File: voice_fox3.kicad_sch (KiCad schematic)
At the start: 9 parts, among them J2 SJ1-2503A, J3 SJ1-3533NG, Q1 2N3904, U1 DFR0299

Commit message: added audio in to mcu ADC
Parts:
- added R3, R4: 10K, Resistor_THT:R_Axial_DIN0207_L6.3mm_D2.5mm_P10.16mm_Horizontal, symbol Device:R
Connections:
- net GND: now also R3.2
- net at C1.1: now also A2.J1_1 (A0), R3.1, R4.2
- net at C1.2: now also J2.3
- net +3.3V: now reaches A2.J2_15 (3V3), A2.J2_6 (3V3), U1.1 (VCC)
- net +3.3V: now also A2.J1_11 (3V3), R4.1
- no-connect marks 32 -> 29
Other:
- note added: "Radio Audio In"
- moved on the sheet: A2A, C1

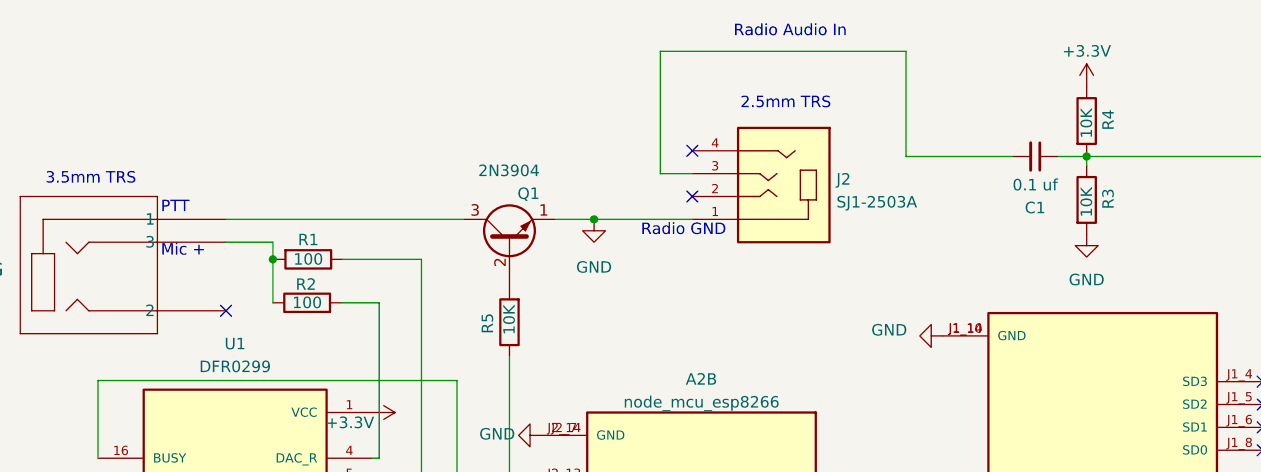
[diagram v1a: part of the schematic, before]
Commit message: added audio in to mcu ADC, added 3v3 net
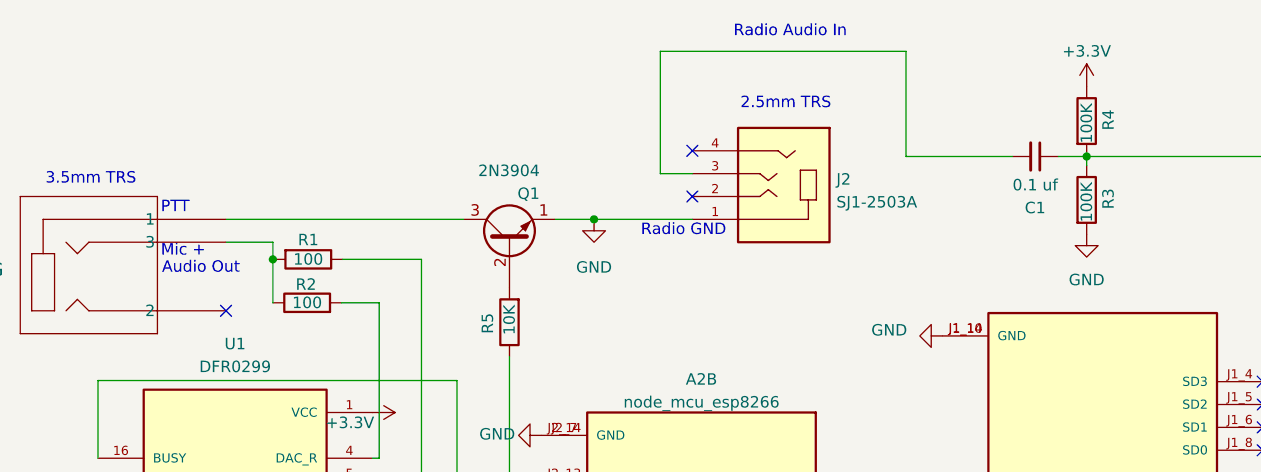
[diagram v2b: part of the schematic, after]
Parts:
- R3, R4: value 10K -> 100K
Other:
- note added: "Audio Out"
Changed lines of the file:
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@@
+    (effects (font (size 1.27 1.27)) (justify left bottom))
+  )
+  (text "Audio Out" (at 81.915 89.789 0)
     (effects (font (size 1.27 1.27)) (justify left bottom))
   )
@@
       (effects (font (size 1.27 1.27)))
     )
-    (property "Value" "10K" (at 184.658 72.898 90)
+    (property "Value" "100K" (at 184.658 72.898 90)
       (effects (font (size 1.27 1.27)))
     )
@@
       (effects (font (size 1.27 1.27)))
     )
-    (property "Value" "10K" (at 184.658 81.661 90)
-      (effects (font (size 1.27 1.27)))
-    )
+    (property "Value" "100K" (at 184.658 81.661 90)
+      (effects (font (size 1.27 1.27)))
+    )

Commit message: many changes
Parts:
- added J1: 2 pin 2mm JST, JST_B2B-PH-K-S(LF)(SN), symbol JST 2pin 2mm jack:B2B-PH-K-S(LF)(SN)
- Q1: footprint Package_TO_SOT_THT:TO-92_Inline -> Package_TO_SOT_THT:TO-92_HandSolder
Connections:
- net GND: now also J1.2
- net at A2.J1_15 (VIN): now also J1.1
- no-connect marks 29 -> 28
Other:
- moved on the sheet: A2A
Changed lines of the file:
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@@
   (junction (at 94.234 88.011) (diameter 0) (color 0 0 0 0)
   )
-  (no_connect (at 204.216 106.68))
+  (no_connect (at 204.851 117.475))
   (no_connect (at 74.803 132.969))
-  (no_connect (at 204.216 124.46))
-  (no_connect (at 204.216 104.14))
-  (no_connect (at 168.656 116.84))
+  (no_connect (at 204.851 135.255))
+  (no_connect (at 204.851 114.935))
+  (no_connect (at 169.291 127.635))
   (no_connect (at 124.079 117.729))
-  (no_connect (at 168.656 119.38))
+  (no_connect (at 169.291 130.175))
   (no_connect (at 74.803 115.189))
   (no_connect (at 74.803 130.429))
@@
   (no_connect (at 159.639 120.269))
   (no_connect (at 105.283 125.349))
-  (no_connect (at 204.216 109.22))
+  (no_connect (at 204.851 120.015))
   (no_connect (at 140.843 75.946))
-  (no_connect (at 204.216 116.84))
+  (no_connect (at 204.851 127.635))
   (no_connect (at 74.803 125.349))
-  (no_connect (at 204.216 114.3))
+  (no_connect (at 204.851 125.095))
   (no_connect (at 159.639 115.189))
   (no_connect (at 74.803 122.809))
-  (no_connect (at 204.216 101.6))
-  (no_connect (at 204.216 127))
+  (no_connect (at 204.851 112.395))
+  (no_connect (at 204.851 137.795))
   (no_connect (at 159.639 122.809))
-  (no_connect (at 168.656 134.62))
   (wire (pts (xy 89.027 86.106) (xy 94.234 86.106))
     (stroke (width 0) (type default))
   )
-  (wire (pts (xy 210.82 119.38) (xy 210.82 76.581))
+  (wire (pts (xy 210.82 130.175) (xy 210.82 76.581))
     (stroke (width 0) (type default))
   )
@@
     (stroke (width 0) (type default))
   )
-  (wire (pts (xy 204.216 119.38) (xy 210.82 119.38))
+  (wire (pts (xy 204.851 130.175) (xy 210.82 130.175))
     (stroke (width 0) (type default))
   )
@@
   )
   (wire (pts (xy 94.234 88.011) (xy 94.361 88.011))
+    (stroke (width 0) (type default))
+  )
+  (wire (pts (xy 152.908 145.415) (xy 169.291 145.415))
     (stroke (width 0) (type default))
   )
@@
     )
   )
-  (symbol (lib_name "GND_2") (lib_id "power:GND") (at 168.656 96.52 270) (unit 1)
-    (in_bom yes) (on_board yes) (dnp no) (fields_autoplaced)
-    (property "Reference" "#PWR02" (at 162.306 96.52 0)
-      (effects (font (size 1.27 1.27)) hide)
-    )
-    (property "Value" "GND" (at 164.719 95.885 90)
+  (symbol (lib_id "power:GND") (at 152.908 142.875 180) (unit 1)
+    (in_bom yes) (on_board yes) (dnp no) (fields_autoplaced)
+    (property "Reference" "#PWR012" (at 152.908 136.525 0)
+      (effects (font (size 1.27 1.27)) hide)
+    )
+    (property "Value" "GND" (at 152.908 138.43 0)
+      (effects (font (size 1.27 1.27)))
+    )
+    (property "Footprint" "" (at 152.908 142.875 0)
+      (effects (font (size 1.27 1.27)) hide)
+    )
+    (property "Datasheet" "" (at 152.908 142.875 0)
+      (effects (font (size 1.27 1.27)) hide)
+    )
+    (pin "1")
+    (instances
+      (project "voice_fox3"
+        (path "/0bd27f7b-372b-41bd-a5d4-e6793a4f4a75"
+          (reference "#PWR012") (unit 1)
+        )
+      )
+    )
+  )
+  (symbol (lib_name "GND_2") (lib_id "power:GND") (at 169.291 107.315 270) (unit 1)
+    (in_bom yes) (on_board yes) (dnp no) (fields_autoplaced)
+    (property "Reference" "#PWR02" (at 162.941 107.315 0)
+      (effects (font (size 1.27 1.27)) hide)
+    )
+    (property "Value" "GND" (at 165.354 106.68 90)
       (effects (font (size 1.27 1.27)) (justify right))
     )
-    (property "Footprint" "" (at 168.656 96.52 0)
-      (effects (font (size 1.27 1.27)) hide)
-    )
-    (property "Datasheet" "" (at 168.656 96.52 0)
+    (property "Footprint" "" (at 169.291 107.315 0)
+      (effects (font (size 1.27 1.27)) hide)
+    )
+    (property "Datasheet" "" (at 169.291 107.315 0)
       (effects (font (size 1.27 1.27)) hide)
     )
@@
   (symbol (lib_id "Device:R") (at 184.658 72.644 0) (unit 1)
     (in_bom yes) (on_board yes) (dnp no)
-    (property "Reference" "R4" (at 187.071 72.517 90)
+    (property "Reference" "R4" (at 182.626 72.517 90)
       (effects (font (size 1.27 1.27)))
     )
@@
     )
   )
-  (symbol (lib_id "power:+3.3V") (at 168.656 132.08 90) (unit 1)
-    (in_bom yes) (on_board yes) (dnp no)
-    (property "Reference" "#PWR09" (at 172.466 132.08 0)
-      (effects (font (size 1.27 1.27)) hide)
-    )
-    (property "Value" "+3.3V" (at 165.735 132.207 90)
+  (symbol (lib_id "JST 2pin 2mm jack:B2B-PH-K-S(LF)(SN)") (at 145.288 145.415 180) (unit 1)
+    (in_bom yes) (on_board yes) (dnp no)
+    (property "Reference" "J1" (at 141.986 145.415 0)
       (effects (font (size 1.27 1.27)) (justify left))
     )
-    (property "Footprint" "" (at 168.656 132.08 0)
-      (effects (font (size 1.27 1.27)) hide)
-    )
-    (property "Datasheet" "" (at 168.656 132.08 0)
+    (property "Value" "2 pin 2mm JST" (at 152.908 149.225 0)
+      (effects (font (size 1.27 1.27)) (justify left))
+    )
+    (property "Footprint" "JST_B2B-PH-K-S(LF)(SN)" (at 145.288 145.415 0)
+      (effects (font (size 1.27 1.27)) (justify bottom) hide)
+    )
+    (property "Datasheet" "" (at 145.288 145.415 0)
+      (effects (font (size 1.27 1.27)) hide)
+    )
+    (property "MF" "JST Sales" (at 145.288 145.415 0)
+      (effects (font (size 1.27 1.27)) (justify bottom) hide)
+    )
+    (property "DIGI-KEY_PURCHASE_URL" "https://www.digikey.com.ua/product-detail/en/jst-sales-america-inc/B2B-PH-K-S_LF__SN_/455-1704-ND/926611?utm_source=snapeda&utm_medium=aggregator&utm_campaign=symbol" (at 145.288 145.415 0)
+      (effects (font (size 1.27 1.27)) (justify bottom) hide)
+    )
+    (property "DESCRIPTION" "PH Series 2 Position 2 mm Pitch Through Hole Top Entry Shrouded Header" (at 145.288 145.415 0)
+      (effects (font (size 1.27 1.27)) (justify bottom) hide)
+    )
+    (property "PACKAGE" "None" (at 145.288 145.415 0)
+      (effects (font (size 1.27 1.27)) (justify bottom) hide)
+    )
+    (property "STANDARD" "IPC-7251" (at 145.288 145.415 0)
+      (effects (font (size 1.27 1.27)) (justify bottom) hide)
+    )
+    (property "PARTREV" "N/A" (at 145.288 145.415 0)
+      (effects (font (size 1.27 1.27)) (justify bottom) hide)
+    )
+    (property "MP" "B2B-PH-K-S_LF__SN_" (at 145.288 145.415 0)
+      (effects (font (size 1.27 1.27)) (justify bottom) hide)
+    )
+    (property "DIGI-KEY_PART_NUMBER" "455-1704-ND" (at 145.288 145.415 0)
+      (effects (font (size 1.27 1.27)) (justify bottom) hide)
+    )
+    (pin "1")
+    (pin "2")
+    (instances
+      (project "voice_fox3"
+        (path "/0bd27f7b-372b-41bd-a5d4-e6793a4f4a75"
+          (reference "J1") (unit 1)
+        )
+      )
+    )
+  )
+  (symbol (lib_id "power:+3.3V") (at 169.291 142.875 90) (unit 1)
+    (in_bom yes) (on_board yes) (dnp no)
+    (property "Reference" "#PWR09" (at 173.101 142.875 0)
+      (effects (font (size 1.27 1.27)) hide)
+    )
+    (property "Value" "+3.3V" (at 166.37 143.002 90)
+      (effects (font (size 1.27 1.27)) (justify left))
+    )
+    (property "Footprint" "" (at 169.291 142.875 0)
+      (effects (font (size 1.27 1.27)) hide)
+    )
+    (property "Datasheet" "" (at 169.291 142.875 0)
       (effects (font (size 1.27 1.27)) hide)
     )
@@
     )
   )
-  (symbol (lib_id "bills_library:node_mcu_esp8266") (at 186.436 116.84 180) (unit 1)
-    (in_bom yes) (on_board yes) (dnp no) (fields_autoplaced)
-    (property "Reference" "A2" (at 186.436 140.716 0)
-      (effects (font (size 1.27 1.27)))
-    )
-    (property "Value" "node_mcu_esp8266" (at 186.436 138.176 0)
-      (effects (font (size 1.27 1.27)))
-    )
-    (property "Footprint" "bills_library:node_mcu_esp8266" (at 186.436 116.84 0)
-      (effects (font (size 1.27 1.27)) (justify bottom) hide)
-    )
-    (property "Datasheet" "" (at 186.436 116.84 0)
-      (effects (font (size 1.27 1.27)) hide)
-    )
-    (property "PARTREV" "N/A" (at 186.436 116.84 0)
-      (effects (font (size 1.27 1.27)) (justify bottom) hide)
-    )
-    (property "STANDARD" "Manufacturer Recommendations" (at 186.436 116.84 0)
-      (effects (font (size 1.27 1.27)) (justify bottom) hide)
-    )
-    (property "MAXIMUM_PACKAGE_HEIGHT" "N/A" (at 186.436 116.84 0)
-      (effects (font (size 1.27 1.27)) (justify bottom) hide)
-    )
-    (property "MANUFACTURER" "Seeed" (at 186.436 116.84 0)
-      (effects (font (size 1.27 1.27)) (justify bottom) hide)
-    )
-    (property "Sim.Enable" "0" (at 186.436 116.84 0)
+  (symbol (lib_id "bills_library:node_mcu_esp8266") (at 187.071 127.635 180) (unit 1)
+    (in_bom yes) (on_board yes) (dnp no) (fields_autoplaced)
+    (property "Reference" "A2" (at 187.071 151.511 0)
+      (effects (font (size 1.27 1.27)))
+    )
+    (property "Value" "node_mcu_esp8266" (at 187.071 148.971 0)
+      (effects (font (size 1.27 1.27)))
+    )
+    (property "Footprint" "bills_library:node_mcu_esp8266" (at 187.071 127.635 0)
+      (effects (font (size 1.27 1.27)) (justify bottom) hide)
+    )
+    (property "Datasheet" "" (at 187.071 127.635 0)
+      (effects (font (size 1.27 1.27)) hide)
+    )
+    (property "PARTREV" "N/A" (at 187.071 127.635 0)
+      (effects (font (size 1.27 1.27)) (justify bottom) hide)
+    )
+    (property "STANDARD" "Manufacturer Recommendations" (at 187.071 127.635 0)
+      (effects (font (size 1.27 1.27)) (justify bottom) hide)
+    )
+    (property "MAXIMUM_PACKAGE_HEIGHT" "N/A" (at 187.071 127.635 0)
+      (effects (font (size 1.27 1.27)) (justify bottom) hide)
+    )
+    (property "MANUFACTURER" "Seeed" (at 187.071 127.635 0)
+      (effects (font (size 1.27 1.27)) (justify bottom) hide)
+    )
+    (property "Sim.Enable" "0" (at 187.071 127.635 0)
       (effects (font (size 1.27 1.27)) hide)
     )
@@
       (effects (font (size 1.27 1.27)) (justify left))
     )
-    (property "Footprint" "Package_TO_SOT_THT:TO-92_Inline" (at 122.428 81.026 0)
+    (property "Footprint" "Package_TO_SOT_THT:TO-92_HandSolder" (at 122.428 81.026 0)
       (effects (font (size 1.27 1.27) italic) (justify left) hide)
     )
